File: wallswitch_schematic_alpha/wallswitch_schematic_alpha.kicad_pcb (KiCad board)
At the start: 2 copper layers, 10 parts, among them IC1 HLW8012, K1 SANYOU_SRD_Form_C, Q1 BC817DPN, Q2 2N7002, Q3 2N7002, U1 AMS1117-3.3, U2 ESP32-WROOM-32D

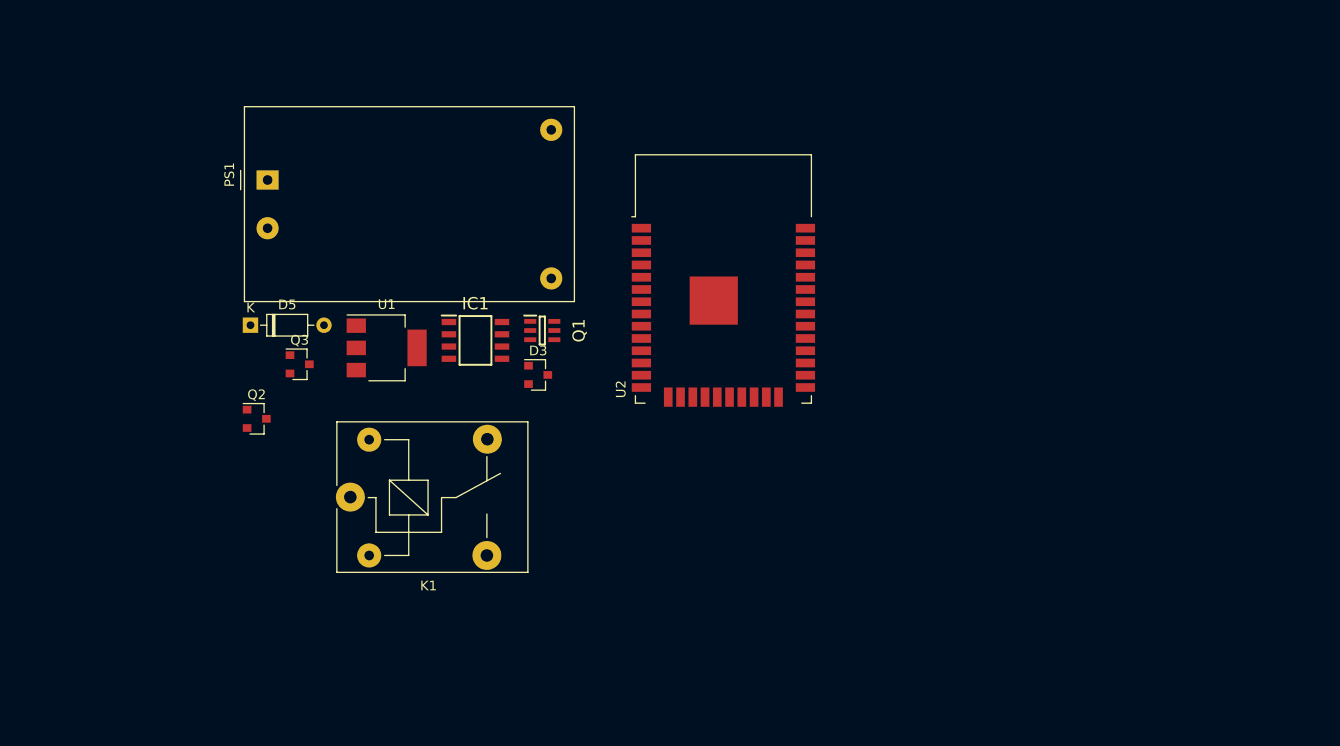
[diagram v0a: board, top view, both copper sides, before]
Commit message: 1. Attached appropriate footprint to connectors 2. TODO: Capacitors and varistor
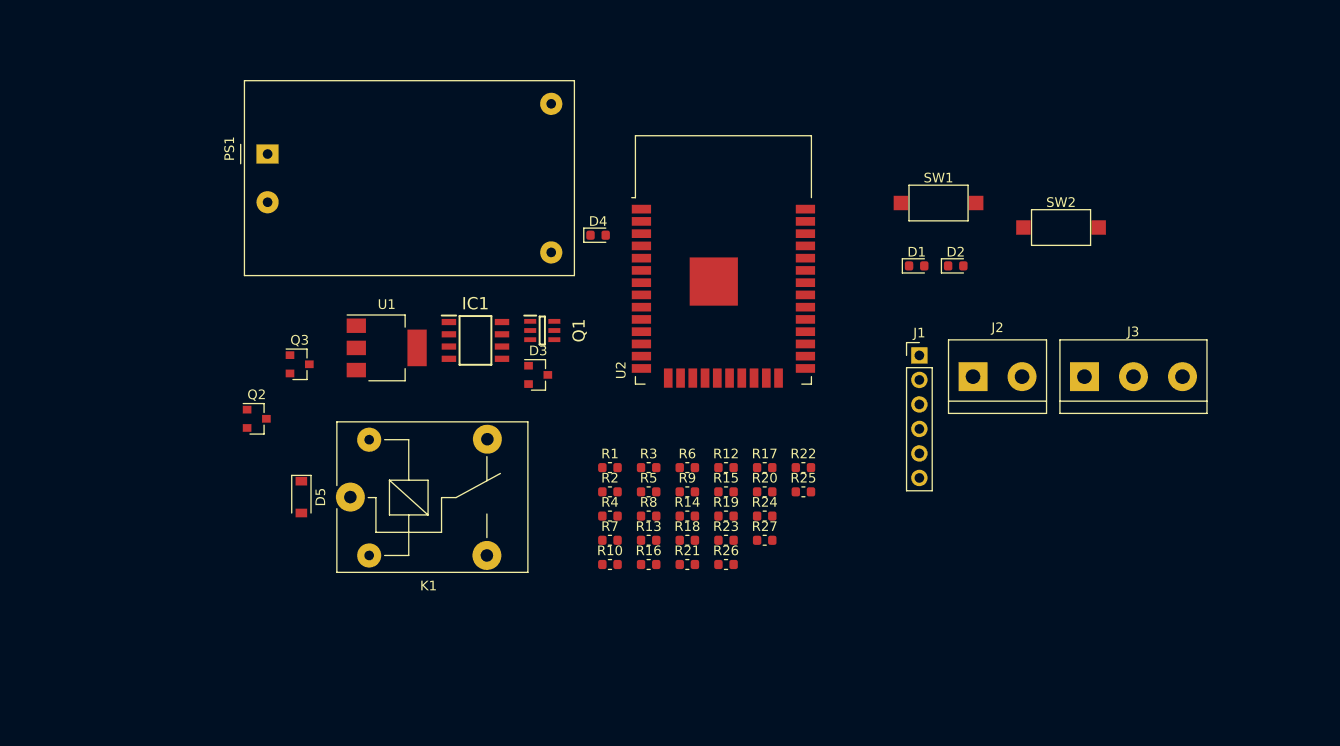
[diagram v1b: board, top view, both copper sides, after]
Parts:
- added D1: LED_5V, LED_SMD:LED_0603_1608Metric, F.Cu at (230.1, 78.9)
- added D2: LED_3V3, LED_SMD:LED_0603_1608Metric, F.Cu at (234.2, 78.9)
- added D4: LED_RELAY, LED_SMD:LED_0603_1608Metric, F.Cu at (197.1, 75.7)
- added J1: Conn_01x06, Connector_PinHeader_2.54mm:PinHeader_1x06_P2.54mm_Vertical, F.Cu at (230.4, 88.2)
- added J2: Screw_Terminal_01x02, TerminalBlock:TerminalBlock_bornier-2_P5.08mm, F.Cu at (236.0, 90.4)
- added J3: Screw_Terminal_01x03, TerminalBlock:TerminalBlock_bornier-3_P5.08mm, F.Cu at (247.5, 90.4)
- added R1: R_12k_±5%_1608m, R_0603_1608Metric, F.Cu at (198.4, 99.8)
- added R10: R_10k_±5%_1608m, R_0603_1608Metric, F.Cu at (198.4, 109.9)
- added R12: R_470k_±1%_1608m, R_0603_1608Metric, F.Cu at (210.4, 99.8)
- added R13: R_470k_±1%_1608m, R_0603_1608Metric, F.Cu at (202.4, 107.3)
- added R14: R_470k_±1%_1608m, R_0603_1608Metric, F.Cu at (206.4, 104.8)
- added R15: R_470k_±1%_1608m, R_0603_1608Metric, F.Cu at (210.4, 102.3)
- added R16: R_470k_±1%_1608m, R_0603_1608Metric, F.Cu at (202.4, 109.9)
- added R17: R_1k_±5%_1608m, R_0603_1608Metric, F.Cu at (214.4, 99.8)
- added R18: R_1k_±5%_1608m, R_0603_1608Metric, F.Cu at (206.4, 107.3)
- added R19: R_0_―_1608m, R_0603_1608Metric, F.Cu at (210.4, 104.8)
- added R2: R_12k_±5%_1608m, R_0603_1608Metric, F.Cu at (198.4, 102.3)
- added R20: R_1.00k_±1%_1608m, R_0603_1608Metric, F.Cu at (214.4, 102.3)
- added R21: R_10k_±5%_1608m, R_0603_1608Metric, F.Cu at (206.4, 109.9)
- added R22: R_10k_±5%_1608m, R_0603_1608Metric, F.Cu at (218.4, 99.8)
- added R23: R_15k_±5%_1608m, R_0603_1608Metric, F.Cu at (210.4, 107.3)
- added R24: R_10k_±5%_1608m, R_0603_1608Metric, F.Cu at (214.4, 104.8)
- added R25: R_15k_±5%_1608m, R_0603_1608Metric, F.Cu at (218.4, 102.3)
- added R26: R_10k_±5%_1608m, R_0603_1608Metric, F.Cu at (210.4, 109.9)
- added R27: R_1k_±5%_1608m, R_0603_1608Metric, F.Cu at (214.4, 107.3)
- added R3: R_1k_±5%_1608m, R_0603_1608Metric, F.Cu at (202.4, 99.8)
- added R4: R_1k_±5%_1608m, R_0603_1608Metric, F.Cu at (198.4, 104.8)
- added R5: R_470_±5%_1608m, R_0603_1608Metric, F.Cu at (202.4, 102.3)
- added R6: R_470_±5%_1608m, R_0603_1608Metric, F.Cu at (206.4, 99.8)
- added R7: R_12k_±5%_1608m, R_0603_1608Metric, F.Cu at (198.4, 107.3)
- added R8: R_1k_±5%_1608m, R_0603_1608Metric, F.Cu at (202.4, 104.8)
- added R9: R_1k_±5%_1608m, R_0603_1608Metric, F.Cu at (206.4, 102.3)
- added SW1: SW_BOOT, Button_Switch_SMD:SW_SPST_CK_RS282G05A3, F.Cu at (232.4, 72.4)
- added SW2: SW_RESET, Button_Switch_SMD:SW_SPST_CK_RS282G05A3, F.Cu at (245.1, 74.9)
- D5: value 1N4148 -> 1N4148W; footprint Diode_THT:D_DO-35_SOD27_P7.62mm_Horizontal -> Diode_SMD:D_SOD-123
- moved D5 18.6 mm to (166.4, 102.9), turned to 270 degrees
- moved PS1 2.70 mm to (162.9, 67.3)
- moved U2 1.98 mm to (210.1, 81.3)

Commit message: progress for layout
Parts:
- added C1: 1n, Capacitor_SMD:C_0603_1608Metric, B.Cu at (214.5, 99.4)
- added C10: 33n, Capacitor_SMD:C_0603_1608Metric, B.Cu at (193.8, 106.5)
- added C11: 0.1u, Capacitor_SMD:C_0603_1608Metric, B.Cu at (191.4, 103.9)
- added C12: 0.1u, Capacitor_SMD:C_0603_1608Metric, B.Cu at (199.0, 101.3)
- added C13: 10u, Capacitor_SMD:C_0603_1608Metric, B.Cu at (200.6, 101.3)
- added C2: 1n, Capacitor_SMD:C_0603_1608Metric, B.Cu at (218.1, 101.0)
- added C3: 10u, Capacitor_SMD:C_0603_1608Metric, B.Cu at (201.5, 86.1)
- added C4: 1n, Capacitor_SMD:C_0603_1608Metric, B.Cu at (221.5, 99.4)
- added C5: 10u, Capacitor_SMD:C_0603_1608Metric, B.Cu at (190.5, 86.1)
- added C6: 10u, Capacitor_SMD:C_0603_1608Metric, B.Cu at (225.1, 101.0)
- added C7: 0.1u, Capacitor_SMD:C_0603_1608Metric, B.Cu at (189.0, 86.1)
- added C8: 0.1u, Capacitor_SMD:C_0603_1608Metric, B.Cu at (225.1, 99.4)
- added C9: 33n, Capacitor_SMD:C_0603_1608Metric, B.Cu at (197.0, 106.5)
- added D10: LED_RELAY, LED_SMD:LED_0603_1608Metric, F.Cu at (159.0, 111.7)
- added D11: 1N4148W, Diode_SMD:D_SOD-123, B.Cu at (177.8, 103.5)
- added D6: LED_USR_1, LED_SMD:LED_0603_1608Metric, F.Cu at (213.9, 94.6)
- added D7: LED_USR_2, LED_SMD:LED_0603_1608Metric, F.Cu at (216.6, 94.6)
- added D8: LED_RELAY, LED_SMD:LED_0603_1608Metric, F.Cu at (154.6, 111.7)
- added D9: 1N4148W, Diode_SMD:D_SOD-123, B.Cu at (161.6, 103.4)
- added F1: Fuse 200mA, Fuse:Fuse_Blade_Mini_directSolder, F.Cu at (164.1, 116.3)
- added H1: MountingHole3.5mm, MountingHole:MountingHole_3.5mm, F.Cu at (232.6, 119.3)
- added H2: MountingHole3.5mm, MountingHole:MountingHole_3.5mm, F.Cu at (240.6, 111.3)
- added J4: Conn_01x06, Connector_PinHeader_2.54mm:PinHeader_1x06_P2.54mm_Vertical, F.Cu at (224.3, 95.0)
- added J5: Screw_Terminal_01x03, TerminalBlock:TerminalBlock_bornier-3_P5.08mm, F.Cu at (156.5, 84.5)
- added J6: Screw_Terminal_01x03, TerminalBlock:TerminalBlock_bornier-3_P5.08mm, F.Cu at (172.7, 84.5)
- added K2: SANYOU_SRD_Form_C, XLAB_Block:Relay_SPDT_SANYOU_SRD_Series_Form_C, F.Cu at (161.6, 107.3)
- added K3: SANYOU_SRD_Form_C, XLAB_Block:Relay_SPDT_SANYOU_SRD_Series_Form_C, F.Cu at (177.7, 107.3)
- added Q4: 2N7002, Package_TO_SOT_SMD:SOT-23, B.Cu at (160.8, 98.4)
- added Q5: 2N7002, Package_TO_SOT_SMD:SOT-23, B.Cu at (177.2, 98.5)
- added R11: 1m, Resistor_SMD:R_2512_6332Metric_Pad1.52x3.35mm_HandSolder, B.Cu at (187.8, 114.5)
- added R28: R_470_±5%_1608m, R_0603_1608Metric, B.Cu at (213.9, 94.6)
- added R29: R_470_±5%_1608m, R_0603_1608Metric, B.Cu at (216.6, 94.6)
- added R30: R_1k_±5%_1608m, R_0603_1608Metric, B.Cu at (154.6, 111.7)
- added R31: R_1k_±5%_1608m, R_0603_1608Metric, B.Cu at (162.7, 101.2)
- added R32: R_10k_±5%_1608m, R_0603_1608Metric, B.Cu at (163.6, 98.6)
- added R33: R_1k_±5%_1608m, R_0603_1608Metric, B.Cu at (159.0, 111.7)
- added R34: R_1k_±5%_1608m, R_0603_1608Metric, B.Cu at (179.0, 101.3)
- added R35: R_10k_±5%_1608m, R_0603_1608Metric, B.Cu at (179.9, 98.8)
- added REF**: OSHW-Logo_5.7x6mm_SilkScreen, Symbol:OSHW-Logo_5.7x6mm_SilkScreen, F.Cu at (142.4, 112.6)
- added RV1: Varistor 270V, Varistor:RV_Disc_D12mm_W3.9mm_P7.5mm, F.Cu at (165.0, 110.8)
- D3, D5, IC1, Q1, Q2, Q3, R1, R10, R12, R13, R14, R15, R16, R17, R18, R19, R2, R20, R21, R22, R23, R24, R25, R26, R27, R3, R4, R5, R6, R7, R8, R9, U1: moved to B.Cu
- moved J3 107.2 mm to (140.5, 84.5)
- moved R9 59.9 mm to (146.5, 102.1)
- moved D4 59.1 mm to (150.3, 111.7), turned to 90 degrees
- moved J2 58.2 mm to (183.0, 114.5), turned to 180 degrees
- moved PS1 54.6 mm to (193.7, 112.4), turned to 90 degrees
- moved R8 52.6 mm to (150.3, 111.7), turned to 90 degrees
- moved R10 52.1 mm to (147.3, 99.3), turned to 90 degrees
- moved Q3 35.4 mm to (200.5, 97.9), turned to 270 degrees
- moved SW2 31.8 mm to (215.1, 85.3), turned to 270 degrees
- moved U2 28.8 mm to (217.5, 109.1), turned to 270 degrees
- moved D2 27.9 mm to (211.2, 94.6), turned to 90 degrees
- moved D1 26.8 mm to (208.5, 94.6), turned to 90 degrees
- moved K1 26.3 mm to (145.6, 107.3), turned to 90 degrees
- moved SW1 26.0 mm to (209.9, 85.3), turned to 270 degrees
- moved R22 24.8 mm to (193.8, 96.9)
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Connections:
- net /5V_DBG renamed /5V_EXT
- net /AC_LINE_IN_M renamed /AC_LINE_M
- net /EN renamed /EN_RESET
- net /IO0 renamed /BOOT
- net /IO12 renamed /PMONITOR_CF
- net /IO18 renamed Net-(U2-Pad30)
- net /IO19 renamed Net-(U2-Pad31)
- net /IO21 renamed Net-(U2-Pad33)
- net /IO22 renamed Net-(U2-Pad36)
- net /IO23 renamed Net-(U2-Pad37)
- net /IO26 renamed Net-(U2-Pad11)
- net /SCK_CLK renamed Net-(U2-Pad20)
- net /SCS_CMD renamed Net-(U2-Pad19)
- net /SDI_SD1 renamed Net-(U2-Pad22)
- net /SDO_SD0 renamed Net-(U2-Pad21)
- net /SENSOR_VN renamed Net-(U2-Pad5)
- net /SENSOR_VP renamed Net-(U2-Pad4)
- net /SHD_SD2 renamed Net-(U2-Pad17)
- net /SWP_SD3 renamed Net-(U2-Pad18)
- D3 pad 2: /5V_TAP -> +5V
- D3 pad 3: +5V -> Net-(C3-Pad1)
- J2 pad 1: /AC_NEUTRAL -> /AC_LINE_IN
- J2 pad 2: /AC_LINE_IN -> /AC_NEUTRAL
- J3 pad 1: /AC_OUT_NC -> /AC_OUT1_NO
- J3 pad 2: /AC_OUT_NO -> /AC_OUT1_NC
- K1 pad 2: Net-(D4-Pad1) -> +5V
- K1 pad 3: /AC_OUT_NC -> /AC_OUT1_NC
- K1 pad 4: /AC_OUT_NO -> /AC_OUT1_NO
- K1 pad 5: +5V -> Net-(D4-Pad1)
- PS1 pad 3: Net-(C3-Pad2) -> GND
- PS1 pad 4: /5V_TAP -> +5V
- R18 pad 2: /AC_LINE -> /AC_LINE_IN
- R21 pad 1: /IO5 -> /PMONITOR_CF1
- R25 pad 1: /IO5 -> /PMONITOR_CF1
- R27 pad 1: /IO4 -> /PMONITOR_SEL
- R9 pad 2: /IO13 -> /REL1_ON
- U1 pad 3: +5V -> Net-(C3-Pad1)
- U2 pad 10: /IO25 -> /GPIO25
- U2 pad 12: /IO27 -> /PMONITOR_SEL
- U2 pad 13: /IO14 -> /PMONITOR_CF1
- U2 pad 16: /IO13 -> Net-(U2-Pad16)
- U2 pad 23: /IO15 -> /LED_USR_1
- U2 pad 24: /IO2 -> /LED_USR_2
- U2 pad 26: /IO4 -> Net-(U2-Pad26)
- U2 pad 27: /IO16 -> /REL1_ON
- U2 pad 28: /IO17 -> /REL2_ON
- U2 pad 29: /IO5 -> /REL3_ON
- U2 pad 6: /IO34 -> /GPIO34
- U2 pad 7: /IO35 -> /GPIO35
- U2 pad 8: /IO32 -> /GPIO32
- U2 pad 9: /IO33 -> /GPIO33
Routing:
- net Net-(F1-Pad1): track 0.00 -> 35.4 mm
- net Net-(D10-Pad1): track 0.00 -> 24.9 mm, vias 0 -> 1
- net +5V: track 0.00 -> 23.7 mm
- net Net-(D4-Pad1): track 0.00 -> 20.5 mm
- net /AC_LINE_IN: track 0.00 -> 18.0 mm
- net Net-(D8-Pad1): track 0.00 -> 15.6 mm, vias 0 -> 1
- net /AC_OUT2_NC: track 0.00 -> 11.2 mm
- net /AC_OUT1_NC: track 0.00 -> 11.2 mm
- net /AC_OUT3_NC: track 0.00 -> 11.1 mm
- net /EN_RESET: track 0.00 -> 5.94 mm
- net Net-(C11-Pad1): track 0.00 -> 5.80 mm
- net Net-(C3-Pad1): track 0.00 -> 5.77 mm
- net Net-(IC1-Pad8): track 0.00 -> 5.72 mm
- net /BOOT: track 0.00 -> 5.71 mm
- net Net-(Q2-Pad1): track 0.00 -> 4.01 mm
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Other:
- board outline added: 90 x 40 mm
- copper layers 2 -> 4
- board text added: "3V3"
- board text added: "5V"
- board text added: "BOOT"
- board text added: "IoT Wall Switch v0.0 nacansino"
- board text added: "RELAY1"
- board text added: "RELAY2"
- board text added: "RELAY3"
- board text added: "RST_EN"
- board text added: "U1"
- board text added: "U2"

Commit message: finished artwork
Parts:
- added C14: 10u, Capacitor_SMD:C_0603_1608Metric, B.Cu at (203.9, 85.3)
- moved R11 46.3 mm to (141.6, 111.1), turned to 180 degrees
- moved J2 42.6 mm to (140.3, 114.8), turned to 0 degrees
- moved REF** 39.3 mm to (181.6, 114.9)
- moved H2 24.2 mm to (220.6, 125.0)
- moved H1 20.4 mm to (213.0, 125.0)
- moved R1 18.5 mm to (226.0, 107.6), turned to 90 degrees
- moved D10 16.6 mm to (175.3, 114.9)
- moved D4 16.6 mm to (166.6, 114.9)
- moved R33 16.6 mm to (175.3, 114.9)
- moved R8 16.6 mm to (166.6, 114.9)
- moved D8 16.6 mm to (170.9, 114.9)
- moved R30 16.6 mm to (170.9, 114.9)
- moved Q1 16.0 mm to (223.4, 106.9), turned to 90 degrees
- moved C2 13.4 mm to (215.6, 87.8)
- moved R2 12.5 mm to (223.8, 103.9), turned to 0 degrees
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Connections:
- C3 pad 1: Net-(C3-Pad1) -> +5V
- D3 pad 3: Net-(C3-Pad1) -> +5V
- J4 pad 1: /GPIO25 -> /GPIO34
- J4 pad 2: /GPIO33 -> /GPIO35
- J4 pad 4: /GPIO35 -> /GPIO33
- J4 pad 5: /GPIO34 -> /GPIO25
- U1 pad 3: Net-(C3-Pad1) -> +5V
- U2 pad 39: (no net) -> GND
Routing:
- net GND: track 1.60 -> 96.6 mm, vias 0 -> 27
- net /REL1_ON: track 0.00 -> 74.7 mm, vias 0 -> 3
- net /AC_LINE_M: track 0.00 -> 73.7 mm, vias 0 -> 2
- net /AC_LINE_IN: track 18.0 -> 79.6 mm, vias 0 -> 2
- net /REL2_ON: track 0.00 -> 61.5 mm, vias 0 -> 3
- net /REL3_ON: track 0.00 -> 47.3 mm, vias 0 -> 3
- net /BOOT: track 5.71 -> 52.9 mm, vias 0 -> 2
- net +5V: track 23.7 -> 60.2 mm, vias 0 -> 8
- net /RXD: track 0.00 -> 29.4 mm, vias 0 -> 1
- net /EN_RESET: track 5.94 -> 33.2 mm, vias 0 -> 2
- net /TXD: track 0.00 -> 27.0 mm, vias 0 -> 1
- net Net-(D4-Pad1): track 20.5 -> 45.7 mm, vias 0 -> 1
- net /LED_USR_2: track 0.00 -> 24.0 mm, vias 0 -> 1
- net /PMONITOR_CF: track 1.60 -> 24.1 mm, vias 0 -> 1
- net /GPIO25: track 0.00 -> 22.5 mm
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- added copper zone on B.Cu, net +3V3
- added copper zone on In1.Cu, net +3V3
- added copper zone on In1.Cu, net +5V
- added copper zone on B.Cu, net /AC_LINE_M
- added copper zone on In2.Cu, net /AC_NEUTRAL
- added copper zone on B.Cu, net GND
- added copper zone on F.Cu, net GND
- added copper zone on In2.Cu, net GND
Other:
- board text added: "25"
- board text added: "32"
- board text added: "33"
- board text added: "34"
- board text added: "35"
- board text added: "5VE"
- board text added: "DTR"
- board text added: "GND"
- board text added: "IoT Switch version alpha nacansino"
- board text added: "RTS"
- board text added: "RXD"
- board text added: "TXD"
- board text removed: "IoT Wall Switch v0.0 nacansino"

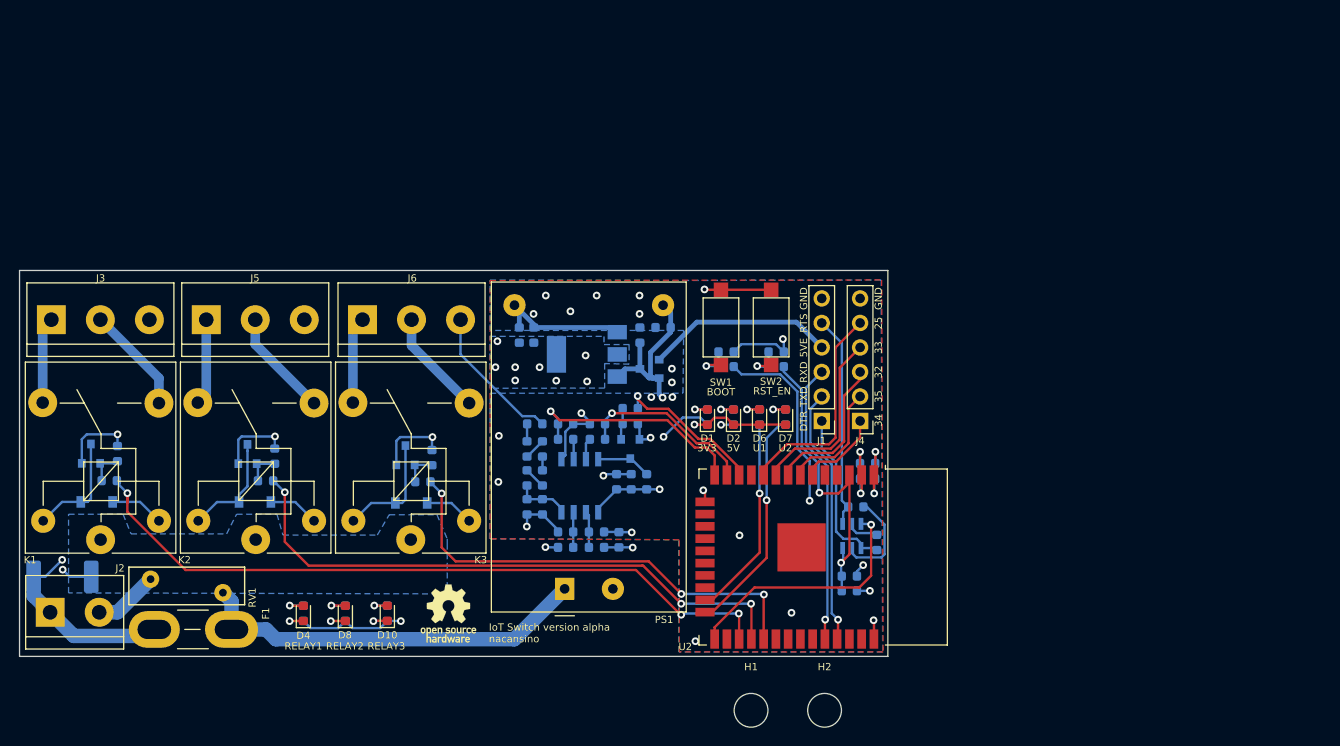
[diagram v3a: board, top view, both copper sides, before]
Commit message: added 3d picture to readme
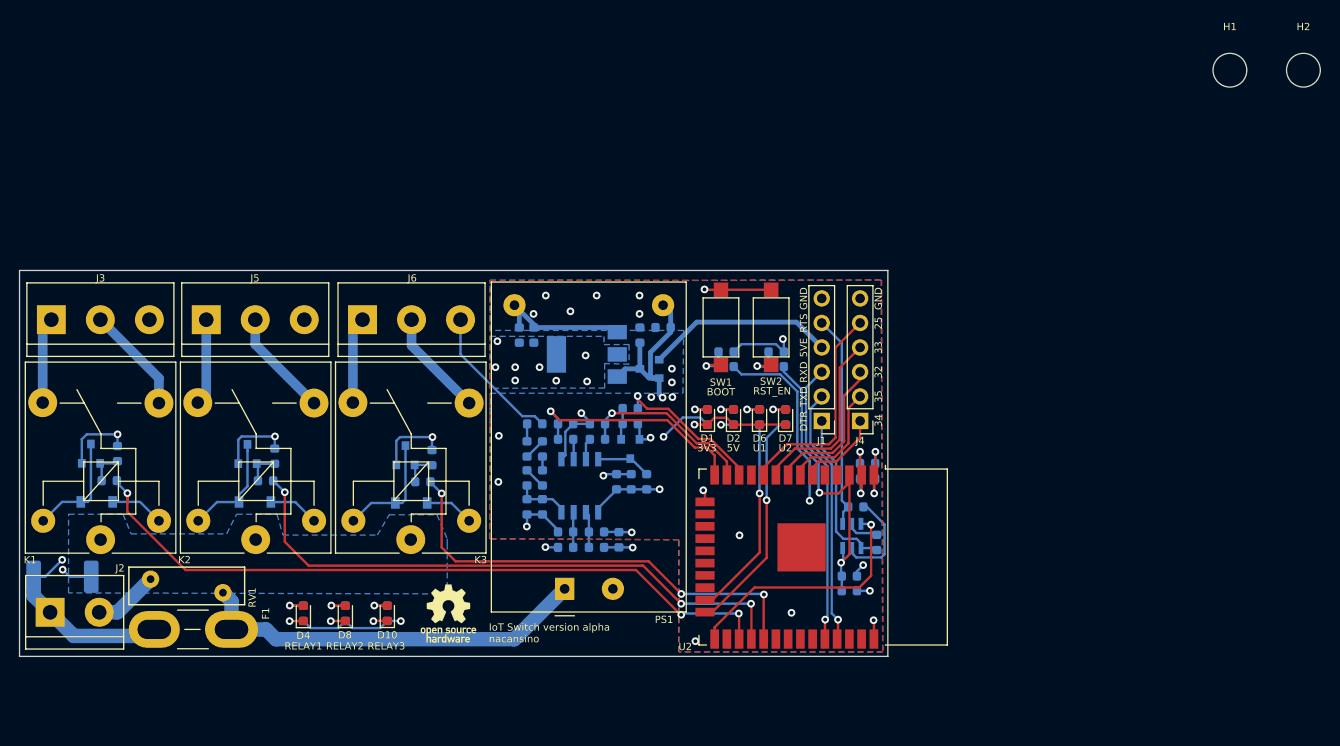
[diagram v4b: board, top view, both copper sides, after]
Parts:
- moved H2 82.9 mm to (270.2, 58.6)
- moved H1 82.9 mm to (262.6, 58.6)

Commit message: modification to generate gerber files
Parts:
- removed H1, H2: MountingHole3.5mm, MountingHole:MountingHole_3.5mm
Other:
- net class Default: via_drill 0.4 -> 0.45
- rule via_min_size: 0.4 -> 0.45
